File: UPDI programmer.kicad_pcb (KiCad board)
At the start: 2 copper layers, 20 x 50 mm, 18 parts, among them J1 USB_C_Receptacle_USB2.0, J2 Conn_01x03, SW1 power, U1 CH340C, U2 MCP1700x-330xxTT

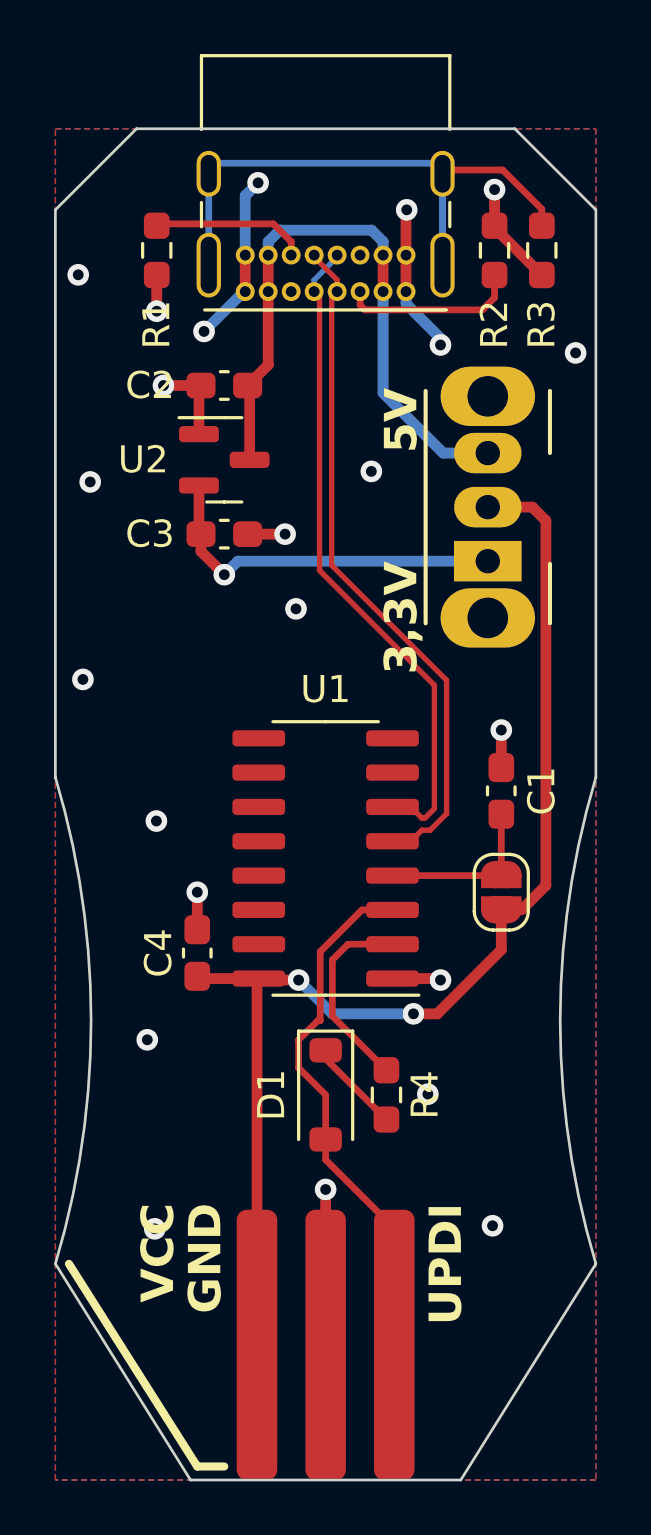
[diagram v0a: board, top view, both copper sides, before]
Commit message: Added panelization files (but there's a problem with tabs. Added fabrication files.
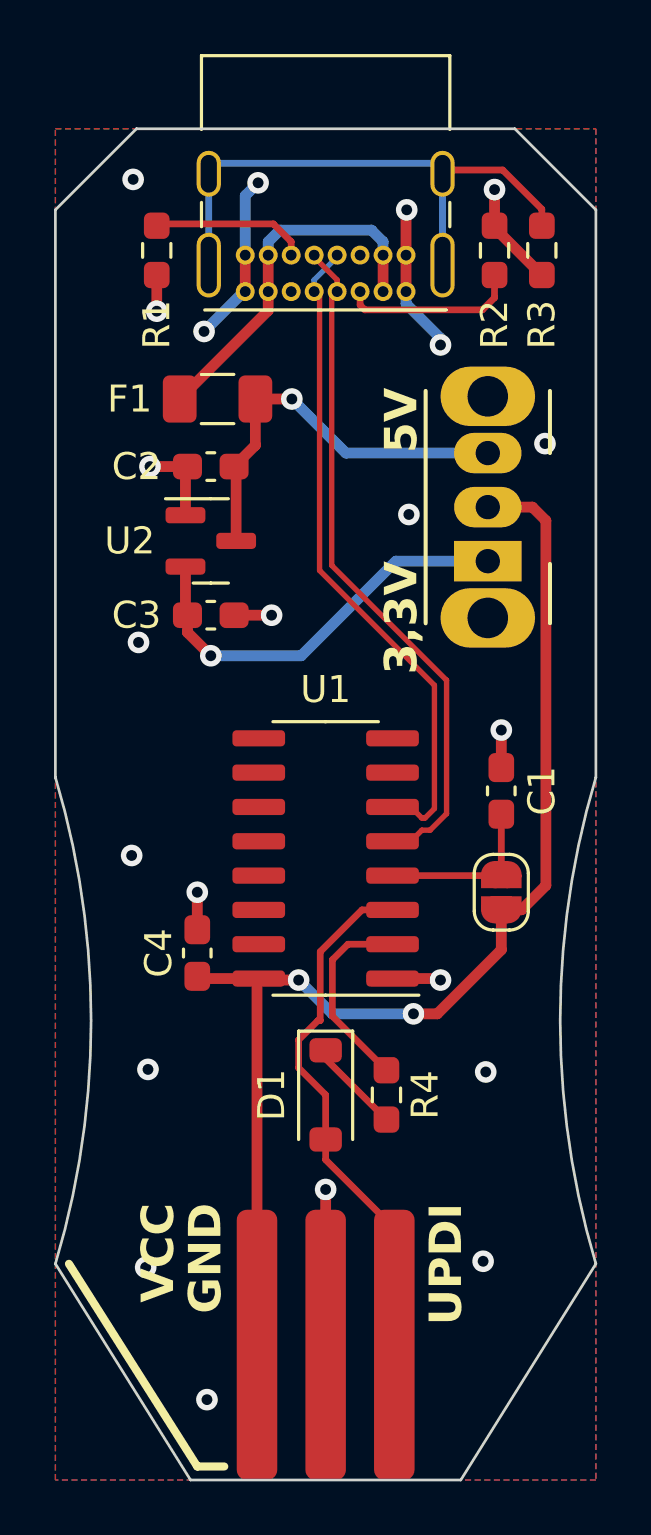
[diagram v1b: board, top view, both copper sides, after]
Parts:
- added F1: 500m, Fuse:Fuse_1206_3216Metric, F.Cu at (156.0, 70.0)
- moved C2 3.04 mm to (155.8, 72.5)
- moved C3 3.04 mm to (155.8, 78.0)
- moved U2 3.04 mm to (155.8, 75.2)
- moved REF** 2.75 mm to (160.0, 55.2)
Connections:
- J1 pad A4: +5V -> Net-(F1-Pad2)
- J1 pad A9: +5V -> Net-(F1-Pad2)
- J1 pad B4: +5V -> Net-(F1-Pad2)
- J1 pad B9: +5V -> Net-(F1-Pad2)
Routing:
- net Net-(F1-Pad2): track 0.00 -> 13.6 mm
- net +5V: track 23.4 -> 15.0 mm, vias 0 -> 1
- net +3.3V: track 13.6 -> 15.4 mm
- net GND: vias 23 -> 22

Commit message: Added version on bottom silk.
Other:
- board text added: "v1.0"
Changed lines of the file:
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@@
     (effects (font (size 1.2 1.2) (thickness 0.15)) (justify left mirror))
+  )
+  (gr_text "v1.0" (at 158.5 83.75 270) (layer "B.SilkS")
+    (effects (font (size 1 1) (thickness 0.15) italic) (justify left mirror))
   )
   (gr_text "UPDI" (at 163.75 99.75 90) (layer "F.SilkS")
